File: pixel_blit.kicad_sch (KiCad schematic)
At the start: 39 parts, among them J1 Conn_01x03_Pin, SW1 K2-1808SN-A4SW, SW2 DSWB04LHGET, U1 RP2350B_C42415655, U2 W25Q128JVSIQTR

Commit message: Checkpoint
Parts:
- removed C16: 4.7uF, PCM_JLCPCB:C_0402, symbol PCM_JLCPCB-Capacitors:0402,4.7uF
- added C16: 4.7uF, PCM_JLCPCB:C_0603, symbol PCM_JLCPCB-Capacitors:0603,4.7uF
- added H1, H2, H3, H4: MountingHole_Pad, MountingHole:MountingHole_3.2mm_M3_Pad_Via, symbol Mechanical:MountingHole_Pad
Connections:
- net +3V3: now also R6.1, U1.64 (VREG_VIN), C16.2
- net 3V3: no longer R6.1, U1.64 (VREG_VIN)
- net GND: now also C17.1, C18.2, X1.2 (GND), X1.4 (GND), C16.1, H1.1, H2.1, H3.1, H4.1
- net at U1.30 (XIN), X1.1: now also C18.1; no longer C17.2
- net at U1.31 (XOUT): now also R9.1; no longer R9.2
- new net: C17.2, R9.2, X1.3
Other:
- moved on the sheet: C17, C18, R9, X1

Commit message: Checkpoint
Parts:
- removed C13: 100nF, EasyEDA:C0402, symbol ProPrj_RP2-easyedapro:UMK105B7104KVHF
- added C13: 100nF, PCM_JLCPCB:C_0402, symbol PCM_JLCPCB-Capacitors:0402,100nF
- added R18: 1kΩ, PCM_JLCPCB:R_0402, symbol PCM_JLCPCB-Resistors:0402,1kΩ
- added SW3, SW4: K2-1808SN-A4SW, EasyEDA:KEY-SMD_4P-L4.2-W3.2-P2.20-LS5.1-TL, symbol EasyEDA:K2-1808SN-A4SW
- added U48, U49: 2.54-1*4, EasyEDA:HDR-TH_4P-P2.54-V-M-1, symbol EasyEDA:2.54-1*4
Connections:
- net 3V3 is gone; now on net +3V3: SW2.5, SW2.6, SW2.7, SW2.8
- net +3V3: now also C13.1, U48.2, U49.1
- net GND: now also C18.1, Reset1.1, Reset1.2, USB1.12 (GND), C13.2, SW3.3, SW3.4, SW4.3, SW4.4, U48.1, U49.2; no longer C18.2, Reset1.3, Reset1.4
- net VBUS: now also D1.2, D2.5
- net at U1.30 (XIN), X1.1: now also C18.2; no longer C18.1
- net SWCLK: now reaches J1.1 (Pin_1), U1.33 (SWCLK)
- net SWDIO: now reaches J1.3 (Pin_3), U1.34 (SWDIO)
- net at U1.35 (RUN): now also R18.1; no longer Reset1.1
- net NEXT_BTN: now reaches U1.56 (GPIO45_ADC5)
- net NEXT_BTN: now also SW4.1, SW4.2
- net DISP_SDA: now reaches U1.57 (GPIO46_ADC6)
- net DISP_SDA: now also U48.3, U49.3
- net DISP_SDL: now reaches U1.58 (GPIO47_ADC7)
- net DISP_SDL: now also U48.4, U49.4
- net USB_D-: now reaches D2.6, U1.66 (USB_DM)
- net USB_D+: now reaches D2.4, U1.67 (USB_DP)
- net USB_SH_D-: now reaches D2.1, USB1.5 (DN2), USB1.7 (DN1)
- net USB_SH_D+: now reaches D2.3, USB1.6 (DP1), USB1.8 (DP2)
- net AUDIO_IN: no longer names the net of U1.54 (GPIO43_ADC3)
- net DATA renamed SELECT_BTN
- net SELECT_BTN: now also SW3.1, SW3.2
- net STATUS: no longer names the net of U1.49 (GPIO40_ADC0)
- new net: R18.2, Reset1.3, Reset1.4
- no-connect marks 3 -> 4
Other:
- note added: "Display Connector"
- moved on the sheet: C18

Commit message: Close to final, lots of cleanup, added back audio
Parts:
- removed R2, R3, R4, R5: 10kΩ, PCM_JLCPCB:R_0603, symbol PCM_JLCPCB-Resistors:0603,10kΩ
- removed SW3, SW4: K2-1808SN-A4SW, EasyEDA:KEY-SMD_4P-L4.2-W3.2-P2.20-LS5.1-TL, symbol EasyEDA:K2-1808SN-A4SW
- removed U48, U49: 2.54-1*4, EasyEDA:HDR-TH_4P-P2.54-V-M-1, symbol EasyEDA:2.54-1*4
- added C42: 22nF, PCM_JLCPCB:C_0402, symbol PCM_JLCPCB-Capacitors:0402,22nF
- added R2, R55: 47kΩ, PCM_JLCPCB:R_0402, symbol PCM_JLCPCB-Resistors:0402,47kΩ
- added R3: 100kΩ, PCM_JLCPCB:R_0402, symbol PCM_JLCPCB-Resistors:0402,100kΩ
- added R4: 220kΩ, PCM_JLCPCB:R_0402, symbol PCM_JLCPCB-Resistors:0402,220kΩ
- added R5: 470kΩ, PCM_JLCPCB:R_0402, symbol PCM_JLCPCB-Resistors:0402,470kΩ
- added R56: 1kΩ, PCM_JLCPCB:R_0402, symbol PCM_JLCPCB-Resistors:0402,1kΩ
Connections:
- net +3V3: now also R55.1; no longer SW2.5, SW2.6, SW2.7, SW2.8
- net GND: now also C42.2, R2.2, R3.2, R4.2, R5.2
- net HS_DATA0: now also U1.44 (GPIO35); no longer U1.77 (GPIO0)
- net HS_DATA1: now also U1.43 (GPIO34); no longer U1.78 (GPIO1)
- net HS_DATA2: now also U1.42 (GPIO33); no longer U1.80 (GPIO3)
- net HS_DATA3: now also U1.40 (GPIO32); no longer U1.79 (GPIO2)
- net SELECT_BTN: now also U1.54 (GPIO43_ADC3); no longer U1.52 (GPIO41_ADC1)
- net STRING0: now also U1.77 (GPIO0); no longer U1.1 (GPIO4)
- net STRING1: now also U1.78 (GPIO1); no longer U1.2 (GPIO5)
- net STRING10: now also U1.8 (GPIO10); no longer U1.13 (GPIO14)
- net STRING11: now also U1.9 (GPIO11); no longer U1.14 (GPIO15)
- net STRING12: now also U1.11 (GPIO12); no longer U1.16 (GPIO16)
- net STRING13: now also U1.12 (GPIO13); no longer U1.17 (GPIO17)
- net STRING14: now also U1.13 (GPIO14); no longer U1.18 (GPIO18)
- net STRING15: now also U1.14 (GPIO15); no longer U1.19 (GPIO19)
- net STRING16: now also U1.16 (GPIO16); no longer U1.20 (GPIO20)
- net STRING17: now also U1.17 (GPIO17); no longer U1.21 (GPIO21)
- net STRING18: now also U1.18 (GPIO18); no longer U1.22 (GPIO22)
- net STRING19: now also U1.19 (GPIO19); no longer U1.23 (GPIO23)
- net STRING2: now also U1.79 (GPIO2); no longer U1.3 (GPIO6)
- net STRING20: now also U1.20 (GPIO20); no longer U1.25 (GPIO24)
- net STRING21: now also U1.21 (GPIO21); no longer U1.26 (GPIO25)
- net STRING22: now also U1.22 (GPIO22); no longer U1.27 (GPIO26)
- net STRING23: now also U1.23 (GPIO23); no longer U1.28 (GPIO27)
- net STRING24: now also U1.25 (GPIO24); no longer U1.36 (GPIO28)
- net STRING25: now also U1.26 (GPIO25); no longer U1.37 (GPIO29)
- net STRING26: now also U1.27 (GPIO26); no longer U1.38 (GPIO30)
- net STRING27: now also U1.28 (GPIO27); no longer U1.39 (GPIO31)
- net STRING28: now also U1.36 (GPIO28); no longer U1.40 (GPIO32)
- net STRING29: now also U1.37 (GPIO29); no longer U1.42 (GPIO33)
- net STRING3: now also U1.80 (GPIO3); no longer U1.4 (GPIO7)
- net STRING30: now also U1.38 (GPIO30); no longer U1.43 (GPIO34)
- net STRING31: now also U1.39 (GPIO31); no longer U1.44 (GPIO35)
- net STRING4: now also U1.1 (GPIO4); no longer U1.6 (GPIO8)
- net STRING5: now also U1.2 (GPIO5); no longer U1.7 (GPIO9)
- net STRING6: now also U1.3 (GPIO6); no longer U1.8 (GPIO10)
- net STRING7: now also U1.4 (GPIO7); no longer U1.9 (GPIO11)
- net STRING8: now also U1.6 (GPIO8); no longer U1.11 (GPIO12)
- net STRING9: now also U1.7 (GPIO9); no longer U1.12 (GPIO13)
- net at SW2.4: now also R2.1; no longer U1.45 (GPIO36)
- net at SW2.3: now also R3.1; no longer U1.46 (GPIO37)
- net at SW2.2: now also R4.1; no longer U1.47 (GPIO38)
- net at SW2.1: now also R5.1; no longer U1.48 (GPIO39)
- net at U1.49 (GPIO40_ADC0): now also C42.1, R56.2
- new net: R55.2, R56.1, SW2.5, SW2.6, SW2.7, SW2.8
- new net AUDIO_IN: U1.52 (GPIO41_ADC1)
- new net SD_CS#: U1.46 (GPIO37)
- new net SD_MISO: U1.45 (GPIO36)
- new net SD_MOSI: U1.48 (GPIO39)
- new net SD_SCK: U1.47 (GPIO38)
- no-connect marks 4 -> 2
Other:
- added sheet Peripherals (peripherals.kicad_sch)
- note removed: "Display Connector"
- moved on the sheet: C14, C15, C16, L1, R18, R6, Reset1, TP1

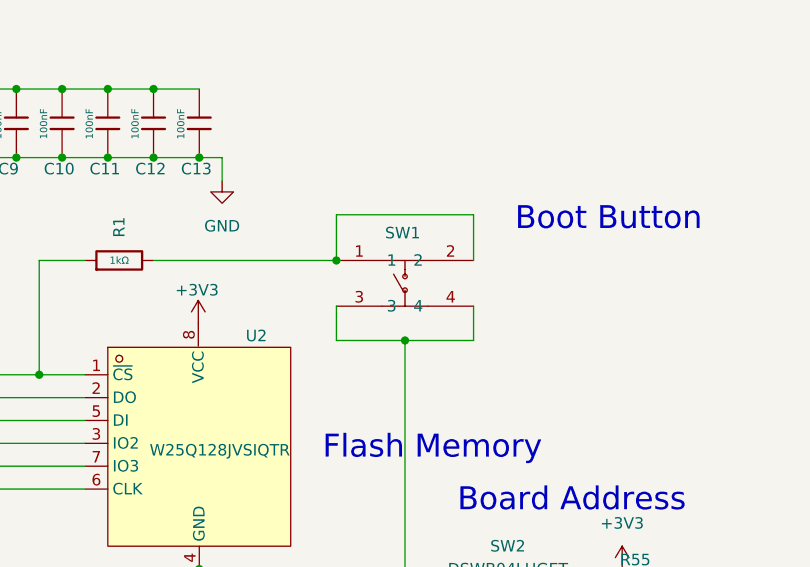
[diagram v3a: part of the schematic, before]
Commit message: Library shuffle and Fabrication Toolkit micro adjustments
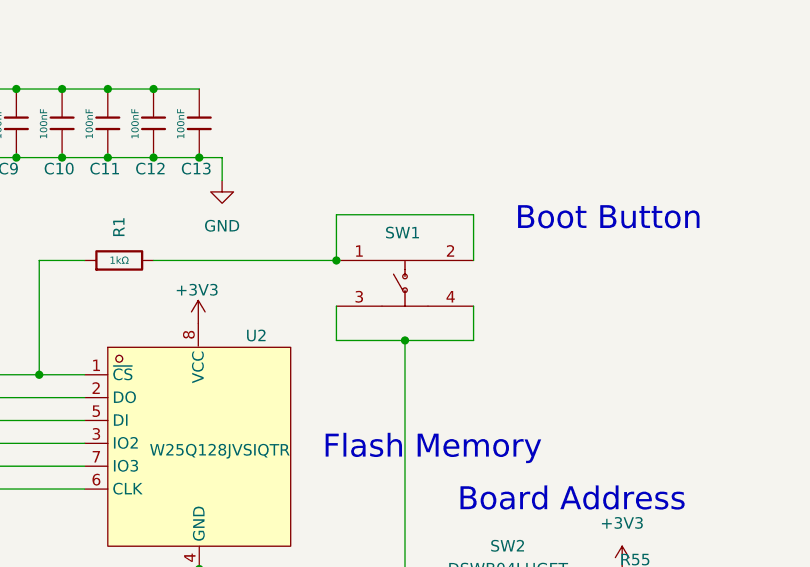
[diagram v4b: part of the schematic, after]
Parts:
- C1, C10, C11, C12, C13, C2, C3, C4, C5, C6, C7, C8, C9: footprint PCM_JLCPCB:C_0402 -> PixelBlit:C_0402; symbol PCM_JLCPCB-Capacitors:0402,100nF -> PixelBlit:0402,100nF
- C14: footprint PCM_JLCPCB:C_0402 -> PixelBlit:C_0402; symbol PCM_JLCPCB-Capacitors:0402,4.7uF -> PixelBlit:0402,4.7uF
- C15, C16: footprint PCM_JLCPCB:C_0603 -> PixelBlit:C_0603; symbol PCM_JLCPCB-Capacitors:0603,4.7uF -> PixelBlit:0603,4.7uF
- C17: footprint EasyEDA:C0402 -> PixelBlit:C0402; symbol EasyEDA:0402CG150J500NT -> PixelBlit:0402CG150J500NT
- C18: footprint EasyEDA:C0402 -> PixelBlit:C0402; symbol EasyEDA:0402CG150J500NT -> PixelBlit:0402CG150J500NT_1
- C42: footprint PCM_JLCPCB:C_0402 -> PixelBlit:C_0402; symbol PCM_JLCPCB-Capacitors:0402,22nF -> PixelBlit:0402,22nF
- D1: footprint PCM_JLCPCB:D_SOD-123 -> PixelBlit:D_SOD-123; symbol PCM_JLCPCB-Diodes:Schottky,B5819W -> PixelBlit:Schottky,B5819W
- D2: footprint EasyEDA:SOT-23-6_L2.9-W1.6-P0.95-LS2.8-BL -> PixelBlit:SOT-23-6_L2.9-W1.6-P0.95-LS2.8-BL; symbol EasyEDA:USBLC6-2SC6 -> PixelBlit:USBLC6-2SC6
- H1, H2, H3, H4: footprint MountingHole:MountingHole_3.2mm_M3_Pad_Via -> PixelBlit:MountingHole_3.2mm_M3_Pad_Via; symbol Mechanical:MountingHole_Pad -> PixelBlit:MountingHole_Pad
- J1: footprint Connector_PinHeader_2.54mm:PinHeader_1x03_P2.54mm_Vertical -> PixelBlit:PinHeader_1x03_P2.54mm_Vertical; symbol Connector:Conn_01x03_Pin -> PixelBlit:Conn_01x03_Pin
- L1: footprint EasyEDA:IND-SMD_L2.0-W1.6_AOTA-B201610S3R3-101-T -> PixelBlit:IND-SMD_L2.0-W1.6_AOTA-B201610S3R3-101-T; symbol ProPrj_RP2-easyedapro:AOTA-B201610S3R3-101-T -> PixelBlit:AOTA-B201610S3R3-101-T
- R1, R18: footprint PCM_JLCPCB:R_0402 -> PixelBlit:R_0402; symbol PCM_JLCPCB-Resistors:0402,1kΩ -> PixelBlit:0402,1kΩ
- R2, R55: footprint PCM_JLCPCB:R_0402 -> PixelBlit:R_0402; symbol PCM_JLCPCB-Resistors:0402,47kΩ -> PixelBlit:0402,47kΩ
- R3: footprint PCM_JLCPCB:R_0402 -> PixelBlit:R_0402; symbol PCM_JLCPCB-Resistors:0402,100kΩ -> PixelBlit:0402,100kΩ
- R4: footprint PCM_JLCPCB:R_0402 -> PixelBlit:R_0402; symbol PCM_JLCPCB-Resistors:0402,220kΩ -> PixelBlit:0402,220kΩ
- R5: footprint PCM_JLCPCB:R_0402 -> PixelBlit:R_0402; symbol PCM_JLCPCB-Resistors:0402,470kΩ -> PixelBlit:0402,470kΩ
- R56: footprint PCM_JLCPCB:R_0402 -> PixelBlit:R_0402; symbol PCM_JLCPCB-Resistors:0402,1kΩ -> PixelBlit:0402,1kΩ_1
- R6: footprint EasyEDA:R0402 -> PixelBlit:R0402; symbol ProPrj_RP2-easyedapro:RT0402BRD0733RL -> PixelBlit:RT0402BRD0733RL
- R7, R8: footprint PCM_JLCPCB:R_0402 -> PixelBlit:R_0402; symbol PCM_JLCPCB-Resistors:0402,5.1kΩ -> PixelBlit:0402,5.1kΩ
- R9: footprint PCM_JLCPCB:R_0603 -> PixelBlit:R_0603; symbol PCM_JLCPCB-Resistors:0603,1kΩ -> PixelBlit:0603,1kΩ
- Reset1: footprint EasyEDA:KEY-SMD_4P-L4.2-W3.2-P2.20-LS5.1-TL -> PixelBlit:KEY-SMD_4P-L4.2-W3.2-P2.20-LS5.1-TL; symbol ProPrj_RP2-easyedapro:K2-1808SN-A4SW -> PixelBlit:K2-1808SN-A4SW
- SW1: footprint EasyEDA:KEY-SMD_4P-L4.2-W3.2-P2.20-LS5.1-TL -> PixelBlit:KEY-SMD_4P-L4.2-W3.2-P2.20-LS5.1-TL; symbol EasyEDA:K2-1808SN-A4SW -> PixelBlit:K2-1808SN-A4SW
- SW2: footprint EasyEDA:SW-TH_DSWB04LHGET -> PixelBlit:SW-TH_DSWB04LHGET; symbol EasyEDA:DSWB04LHGET -> PixelBlit:DSWB04LHGET
- TP1: footprint TestPoint:TestPoint_Pad_1.0x1.0mm -> PixelBlit:TestPoint_Pad_1.0x1.0mm; symbol Connector:TestPoint -> PixelBlit:TestPoint
- U1: footprint EasyEDA:QFN-80_L10.0-W10.0-P0.40-TL-EP3.4 -> PixelBlit:QFN-80_L10.0-W10.0-P0.40-TL-EP3.4; symbol EasyEDA:RP2350B_C42415655 -> PixelBlit:RP2350B_C42415655
- U2: footprint EasyEDA:SOIC-8_L5.3-W5.3-P1.27-LS8.0-BL -> PixelBlit:SOIC-8_L5.3-W5.3-P1.27-LS8.0-BL; symbol EasyEDA:W25Q128JVSIQTR -> PixelBlit:W25Q128JVSIQTR
- USB1: footprint EasyEDA:USB-C-SMD_TYPE-C-6PIN-2MD-073 -> PixelBlit:USB-C-SMD_TYPE-C-6PIN-2MD-073; symbol EasyEDA:TYPE-C16PIN2MD(073) -> PixelBlit:TYPE-C16PIN2MD(073)
- X1: footprint EasyEDA:CRYSTAL-SMD_4P-L3.2-W2.5-BL -> PixelBlit:CRYSTAL-SMD_4P-L3.2-W2.5-BL; symbol ProPrj_RP2-easyedapro:X252012MMB4SI-24 -> PixelBlit:X252012MMB4SI-24
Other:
- moved on the sheet: SW1

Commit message: Working on errata
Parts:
- removed C42: 22nF, PixelBlit:C_0402, symbol PixelBlit:0402,22nF
- removed R2, R55: 47kΩ, PixelBlit:R_0402, symbol PixelBlit:0402,47kΩ
- removed R3: 100kΩ, PixelBlit:R_0402, symbol PixelBlit:0402,100kΩ
- removed R4: 220kΩ, PixelBlit:R_0402, symbol PixelBlit:0402,220kΩ
- removed R5: 470kΩ, PixelBlit:R_0402, symbol PixelBlit:0402,470kΩ
- removed R56: 1kΩ, PixelBlit:R_0402, symbol PixelBlit:0402,1kΩ_1
- removed SW2: DSWB04LHGET, PixelBlit:SW-TH_DSWB04LHGET, symbol PixelBlit:DSWB04LHGET
- renumbered J1 to J37
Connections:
- net BAK: now reaches U1.49 (GPIO40_ADC0)
- net at U1.72 (QSPI_SD0): now also U2.5 (DI); no longer U2.2 (DO)
- net at U1.74 (QSPI_SD1): now also U2.2 (DO); no longer U2.5 (DI)
- net AUDIO_IN renamed PSH
- net DISP_SDL renamed DISP_SCL
- net NEXT_BTN renamed TRA
- net SELECT_BTN renamed TRB
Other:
- note removed: "Board Address"
